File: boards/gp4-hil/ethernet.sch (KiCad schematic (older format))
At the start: 59 parts, among them J1 BEL_FUSE_0826-1G1T-23-F, J3 XILINX_JTAG_ICESIDE, J4 XILINX_JTAG_ICESIDE, U2 XC7A100T-1FTG256C, U29 TXB0104RUT, U30 TXB0104RUT, U33 125 MHz, U5 KSZ9031RN, U7 25 MHz

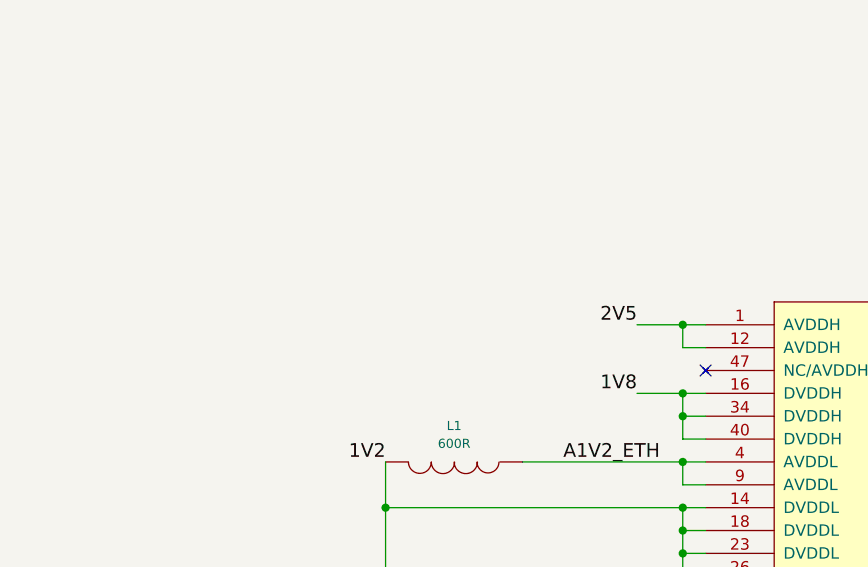
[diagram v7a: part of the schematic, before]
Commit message: Added pi filter to A2V5_ETH for isolation from digital noise
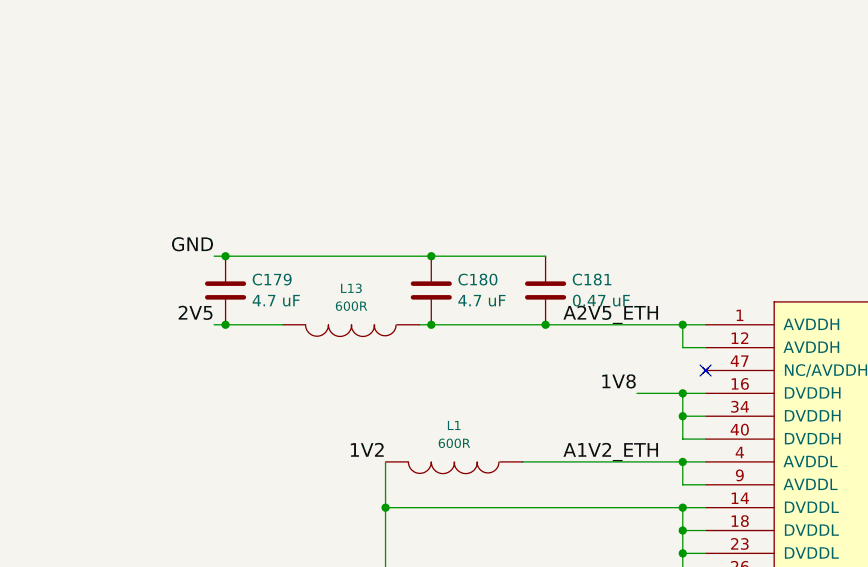
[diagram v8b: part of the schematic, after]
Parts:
- added C179, C180: 4.7 uF, symbol C
- added C181: 0.47 uF, symbol C
- added L13: 600R, symbol INDUCTOR_PWROUT
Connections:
- net 2V5: now also C179.2, L13.2; no longer U5.1 (AVDDH), U5.12 (AVDDH)
- net GND: now also C179.1, C180.1, C181.1
- new net A2V5_ETH: C180.2, C181.2, L13.1, U5.1 (AVDDH), U5.12 (AVDDH)
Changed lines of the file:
@@
 Text Label 8650 6750 2    60   ~ 0
 1V8
-Text Label 8650 6450 2    60   ~ 0
-2V5
+Text Label 8750 6450 2    60   ~ 0
+A2V5_ETH
 NoConn ~ 8950 6650
 Text Label 11400 6650 0    60   ~ 0
@@
 	8850 6550 8950 6550
 Wire Wire Line
-	8650 6450 8950 6450
-Wire Wire Line
 	1800 9000 1650 9000
 Wire Wire Line
@@
 	16000 8500 16200 8500
 NoConn ~ 16200 7400
+$Comp
+L INDUCTOR_PWROUT L13
+U 1 1 5772F580
+P 7400 6450
+F 0 "L13" V 7242 6450 40  0000 C CNN
+F 1 "600R" V 7320 6450 40  0000 C CNN
+F 2 "" H 7400 6450 60  0000 C CNN
+F 3 "" H 7400 6450 60  0000 C CNN
+	1    7400 6450
+	0    1    1    0
+$EndComp
+Text Label 6800 6450 2    60   ~ 0
+2V5
+$Comp
+L C C179
+U 1 1 5772F954
+P 6850 6300
+F 0 "C179" H 6965 6346 50  0000 L CNN
+F 1 "4.7 uF" H 6965 6254 50  0000 L CNN
+F 2 "" H 6888 6150 30  0000 C CNN
+F 3 "" H 6850 6300 60  0000 C CNN
+	1    6850 6300
+	1    0    0    -1
+$EndComp
+Wire Wire Line
+	6800 6450 7100 6450
+Connection ~ 6850 6450
+Text Label 6800 6150 2    60   ~ 0
+GND
+Wire Wire Line
+	6800 6150 8250 6150
+$Comp
+L C C180
+U 1 1 5773003D
+P 7750 6300
+F 0 "C180" H 7865 6346 50  0000 L CNN
+F 1 "4.7 uF" H 7865 6254 50  0000 L CNN
+F 2 "" H 7788 6150 30  0000 C CNN
+F 3 "" H 7750 6300 60  0000 C CNN
+	1    7750 6300
+	1    0    0    -1
+$EndComp
+$Comp
+L C C181
+U 1 1 57730229
+P 8250 6300
+F 0 "C181" H 8365 6346 50  0000 L CNN
+F 1 "0.47 uF" H 8365 6254 50  0000 L CNN
+F 2 "" H 8288 6150 30  0000 C CNN
+F 3 "" H 8250 6300 60  0000 C CNN
+	1    8250 6300
+	1    0    0    -1
+$EndComp
+Wire Wire Line
+	7700 6450 8950 6450
+Connection ~ 7750 6450
+Connection ~ 8250 6450
+Connection ~ 6850 6150
+Connection ~ 7750 6150
 $EndSCHEMATC
